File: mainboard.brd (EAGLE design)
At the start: 90.2 x 95.9 mm, 141 parts, among them J1 503182-1852, J2 10118194-0001LF, J3 DCJ0303, Q1 IRLML2803, Q10 IRLML5103, Q11 IRLML5103, Q12 IRLML5103, Q13 IRLML5103, Q14 IRLML2803, Q15 IRLML2803, Q16 IRLML5103, Q2 IRLML2803, Q5 IRLML2803, Q6 IRLML2803, Q7 IRLML2803, Q8 IRLML2803, Q9 IRLML5103, U1 MAX706R, U12 EP2W+, U13 RFM23BP, U14 S1216V8, U15 XTB_2018_07_15, U16 XTB_2018_07_15, U17 XTB_2018_07_15, U18 XTB_2018_07_15, U2 FXAS21002FXAS21002, U20 MR25H40MDF, U3 LSM9DS1, U4 ATSAMD21G-A, U5 MAX4372TEUK+T, U6 LTC4121-4.2, U7 TPS54226PWPRPWP14_2P31X2P46-L, U8 PE014006, U9 PE014006, X1 BU-SMA-V, X2 BU-SMA-V, X3 BU-SMA-V, Y1 32.768kHz

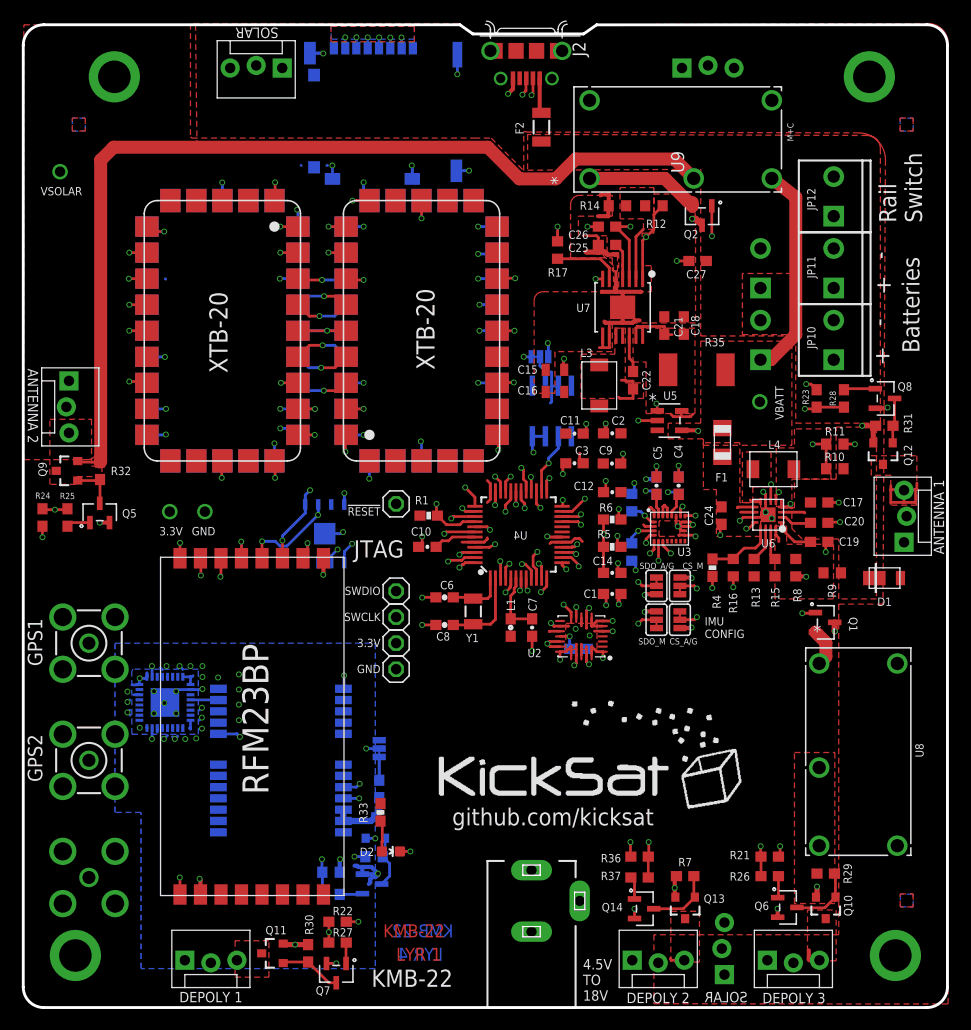
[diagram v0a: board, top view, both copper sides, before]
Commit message: updated mainboard to KMB-23
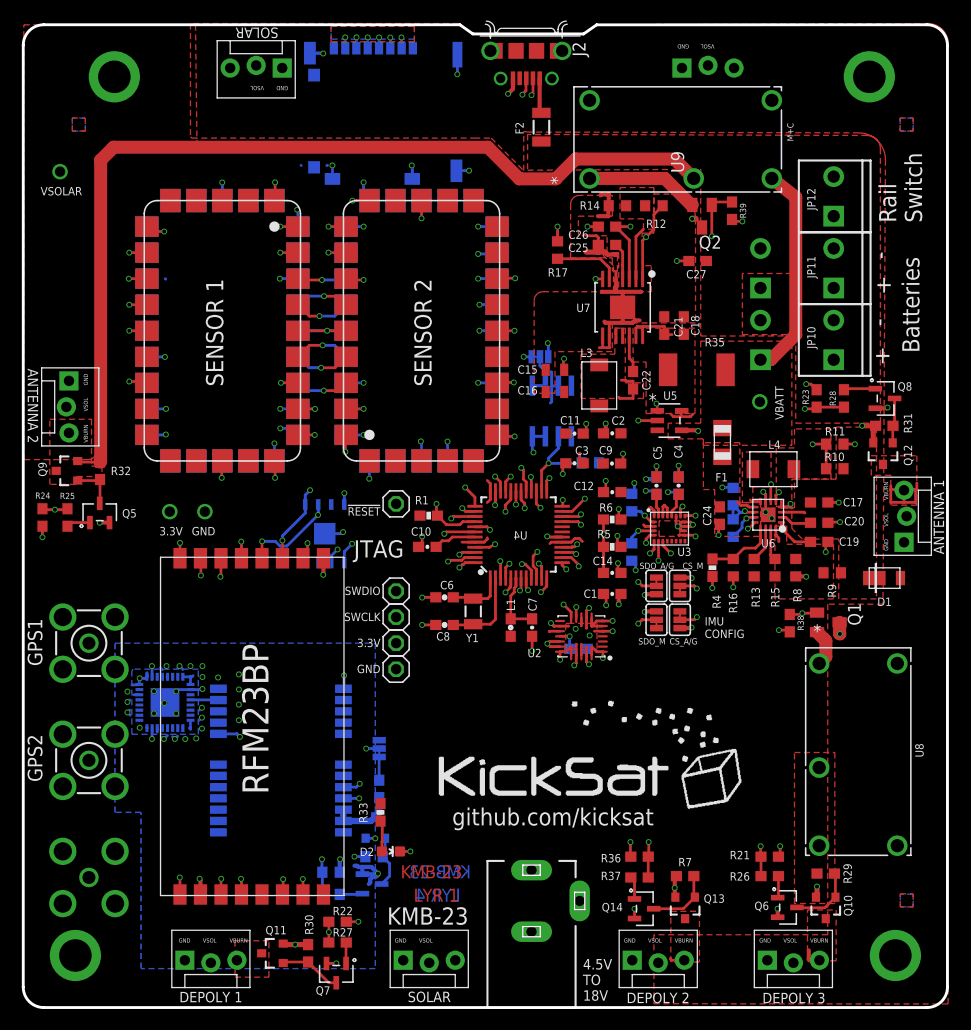
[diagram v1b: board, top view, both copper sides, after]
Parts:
- added R38, R39: 10k, SparkFun-Resistors:0603
- added R40: 2.1M, resistor:R0603
- added R41: 845K, resistor:R0603
- added R42: 10k, resistor:R0603
- C20: value 2.2nF -> 22nF
- Q1, Q2: value IRLML2803 -> BC846; device maholli:SOT-23 -> transistor:SOT23
- moved JP14 31.2 mm to (37.0, 4.50), flipped to the top, turned to 0 degrees
- moved Q1 0.25 mm to (78.5, 37.6)
- moved C24 0.16 mm to (67.9, 48.0)
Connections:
- new net GND4: R39.2
- new net N$31: R40.2, R41.2, U6.P$10
- new net N$49: U13.GPIO_0, U13.RXON
- new net N$54: R41.1, U6.P$11
- new net N$55: U13.GPIO_1, U13.TXON
- net 3.3V: now also U18.P$13, U2.13
- net BURN_RELAY_A: now also R39.1
- net BURN_RELAY_B: now also R38.1
- net GND: now also R38.2, R42.1, U18.P$11; no longer U6.P$11
- net LION1: now also R40.1; no longer U6.P$10
- net N$8: now also U1.1
- net UART1_RX: now also U4.8; no longer U4.7
- net UART1_TX: now also U4.7; no longer U4.8
- net WDT_WDI: now also R42.2
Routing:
- net N$55: track 0.00 -> 11.7 mm, vias 0 -> 2
- net N$49: track 0.00 -> 7.17 mm, vias 0 -> 2
- net N$31: track 0.00 -> 4.87 mm, vias 0 -> 1
- net WDT_WDI: track 6.01 -> 9.24 mm
- net N$54: track 0.00 -> 3.21 mm, vias 0 -> 1
- net BURN_RELAY_A: track 37.0 -> 39.1 mm
- net 3.3V: track 92.5 -> 94.4 mm, vias 27 -> 28
- net BURN_RELAY_B: track 33.5 -> 35.3 mm
- net VSOLAR: track 45.6 -> 47.1 mm
- net N$8: track 3.04 -> 4.31 mm
- net GND: track 210.0 -> 208.8 mm
- net GND4: track 0.00 -> 1.09 mm, vias 0 -> 1
- net VBATT: track 153.1 -> 152.0 mm
- net XTB_RESET: track 55.5 -> 54.5 mm
- net LION1: track 3.15 -> 2.98 mm, vias 0 -> 1
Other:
- board text added: "KMB-23"
- board text added: "SENSOR 1"
- board text added: "SENSOR 2"
- board text added: "SENSOR 3"
- board text added: "SENSOR 4"
- board text added: "VBURN"
- board text added: "VSOL"
- board text removed: "KMB-22"
